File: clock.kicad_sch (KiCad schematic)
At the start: 35 parts, among them U5 NE555P, U6 NE555P

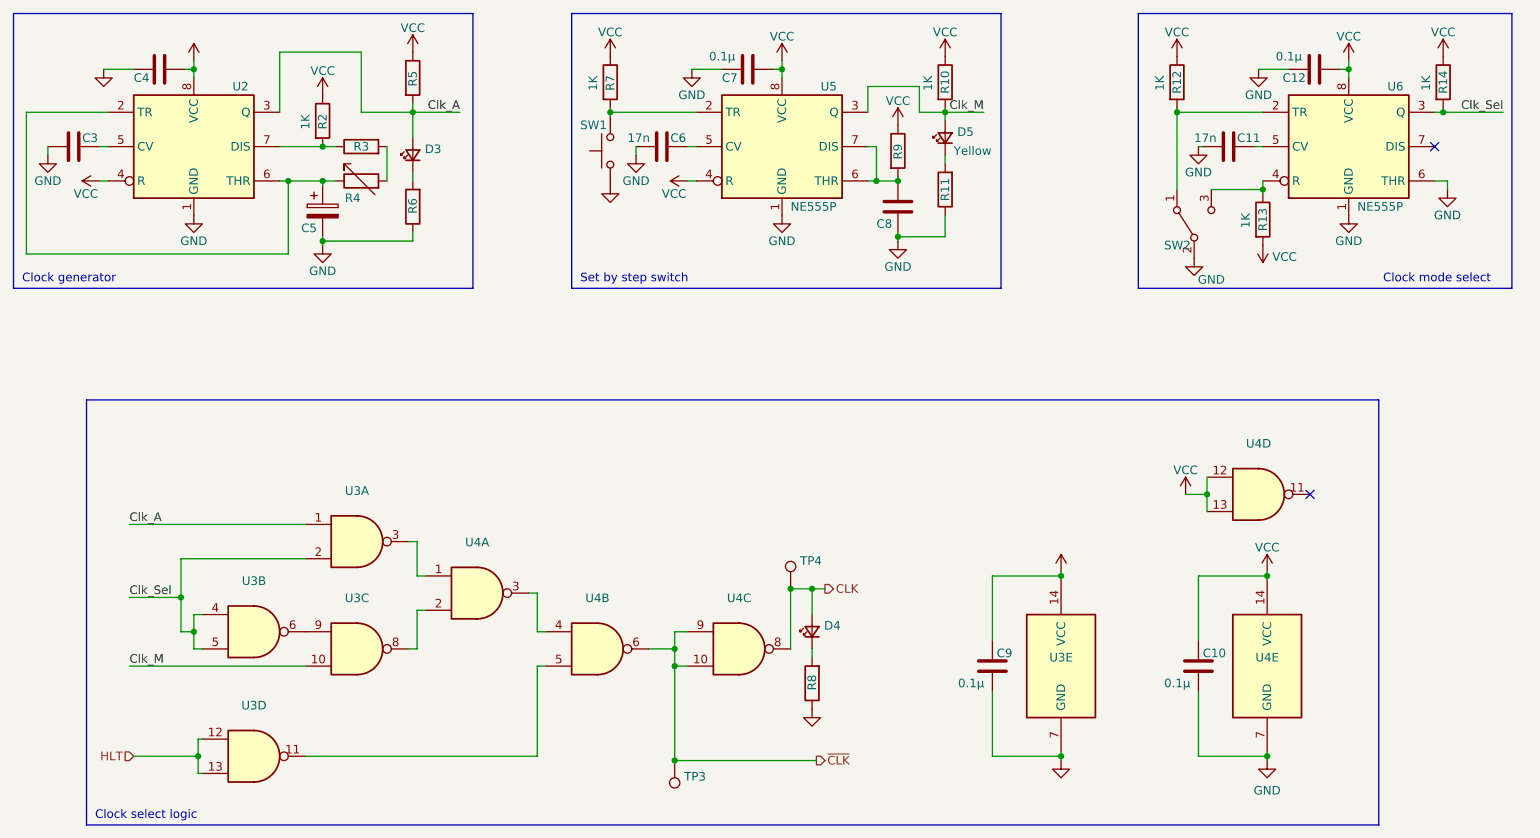
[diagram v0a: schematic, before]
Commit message: 🚧 replace power supply with USB-C socket
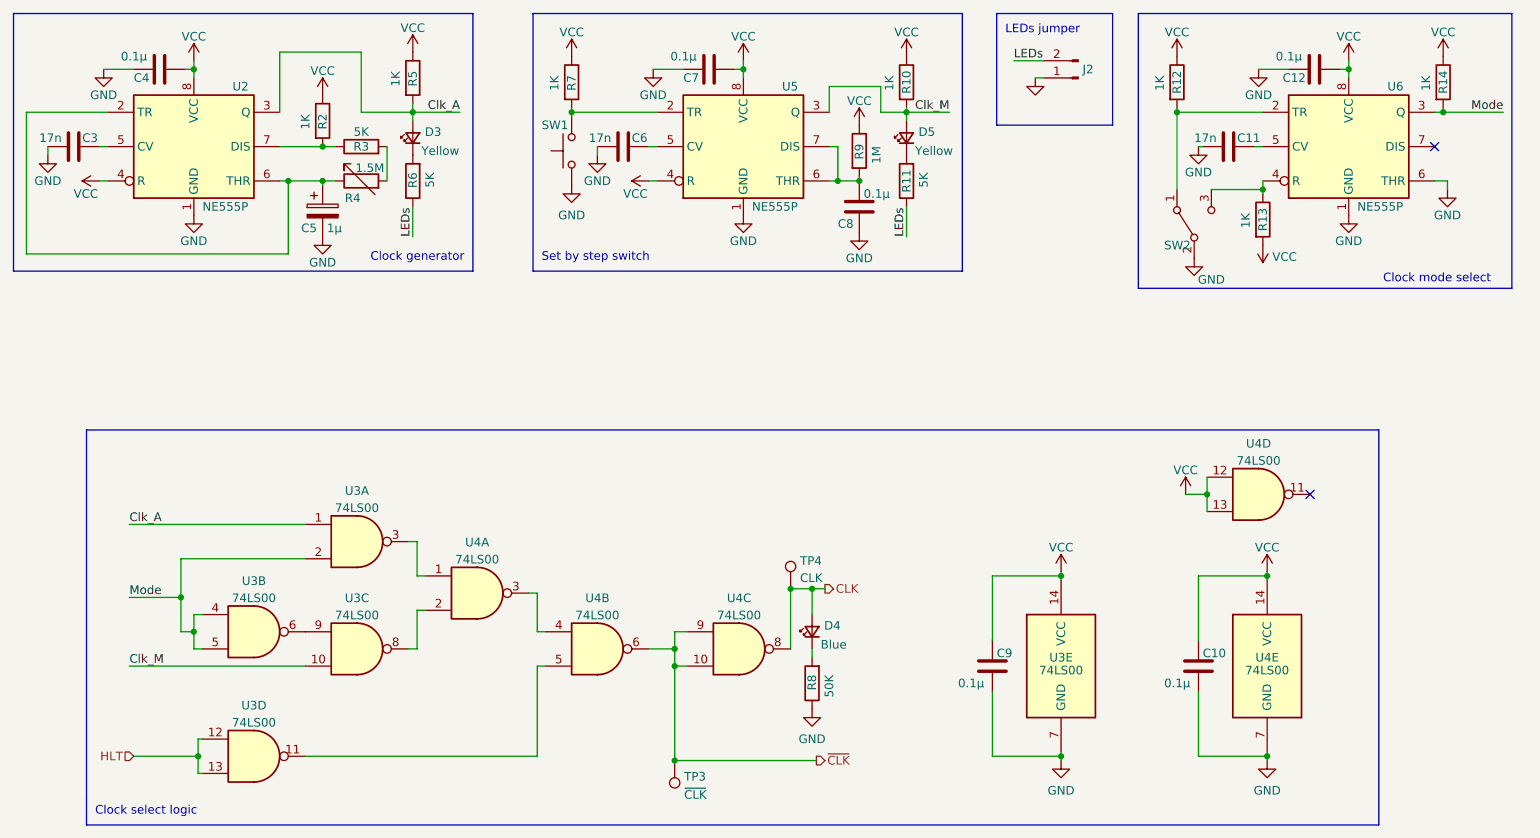
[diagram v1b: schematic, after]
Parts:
- added J2: (no value), symbol Connector:Conn_01x02_Male
- C10, C12, C7, C9: footprint (none) -> Capacitor_THT:C_Rect_L4.6mm_W2.0mm_P2.50mm_MKS02_FKP02
- C11, C6: footprint (none) -> Capacitor_THT:C_Disc_D3.0mm_W1.6mm_P2.50mm
- C3: value (none) -> 17n; footprint (none) -> Capacitor_THT:C_Disc_D3.0mm_W1.6mm_P2.50mm
- C4, C8: value (none) -> 0.1µ; footprint (none) -> Capacitor_THT:C_Rect_L4.6mm_W2.0mm_P2.50mm_MKS02_FKP02
- C5: value (none) -> 1µ; footprint (none) -> Capacitor_THT:CP_Radial_D5.0mm_P2.00mm
- D3: value (none) -> Yellow; footprint (none) -> LED_THT:LED_D5.0mm
- D4: value (none) -> Blue; footprint (none) -> LED_THT:LED_D5.0mm
- D5: footprint (none) -> LED_THT:LED_D5.0mm
- R10, R12, R13, R14, R2, R7: footprint (none) -> Resistor_THT:R_Axial_DIN0204_L3.6mm_D1.6mm_P5.08mm_Horizontal
- R11, R3, R6: value (none) -> 5K; footprint (none) -> Resistor_THT:R_Axial_DIN0204_L3.6mm_D1.6mm_P5.08mm_Horizontal
- R4: value (none) -> 1.5M; footprint (none) -> Potentiometer_THT:Potentiometer_Vishay_T73YP_Vertical
- R5: value (none) -> 1K; footprint (none) -> Resistor_THT:R_Axial_DIN0204_L3.6mm_D1.6mm_P5.08mm_Horizontal
- R8: value (none) -> 50K; footprint (none) -> Resistor_THT:R_Axial_DIN0204_L3.6mm_D1.6mm_P5.08mm_Horizontal
- R9: value (none) -> 1M; footprint (none) -> Resistor_THT:R_Axial_DIN0204_L3.6mm_D1.6mm_P5.08mm_Horizontal
- SW1: value (none) -> Clock step; footprint (none) -> Button_Switch_THT:SW_PUSH_6mm
- TP3: value (none) -> ~{CLK}; footprint (none) -> TestPoint:TestPoint_Loop_D2.60mm_Drill1.4mm_Beaded
- TP4: value (none) -> CLK; footprint (none) -> TestPoint:TestPoint_Loop_D2.60mm_Drill1.4mm_Beaded
- U2: value (none) -> NE555P; footprint (none) -> Package_DIP:DIP-8_W7.62mm
- U3, U4: value (none) -> 74LS00; footprint (none) -> Package_DIP:DIP-14_W7.62mm_LongPads
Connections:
- net GND: now also J2.1 (Pin_1); no longer R11.1, R6.1
- net Clk_Sel renamed Mode
- new net LEDs: J2.2 (Pin_2), R11.1, R6.1
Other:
- note added: "LEDs jumper"
- moved on the sheet: C6, C7, C8, D3, D5, R10, R11, R6, R7, R9, SW1, U5
